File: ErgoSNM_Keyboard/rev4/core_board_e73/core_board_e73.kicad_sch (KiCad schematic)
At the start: 58 parts, among them J1 USB_C_Receptacle_USB2.0, J2 Conn_02x10_Odd_Even, J3 Conn_02x10_Odd_Even, J4 PJ-393_TRRS_8P, J5 PJ-393_TRRS_8P, J6 Conn_Batt, J7 Debug, J8 Conn_02x05_Odd_Even, J9 Conn_02x05_Odd_Even, SW1 SW_SPDT, SW2 SW_SPDT, U1 E73-2G4M08S1C, U2 USBLC6-2SC6, U3 BQ24075RGT, U4 TPS63900, Y1 32.768kHz

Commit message: feat: update E73 core board
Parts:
- removed C1: 4.7nF, Capacitor_SMD:C_0805_2012Metric, symbol Device:C_Small
- removed C10, C9: 4.7uF, Capacitor_SMD:C_0402_1005Metric, symbol Device:C_Small
- removed C11, C12: 22uF, Capacitor_SMD:C_0805_2012Metric, symbol Device:C_Small
- removed C4: 100nF, Capacitor_SMD:C_0402_1005Metric, symbol Device:C_Small
- removed C7: 1uF, Capacitor_SMD:C_0402_1005Metric, symbol Device:C_Small
- removed F1: 500mA, 6V, Fuse:Fuse_0805_2012Metric, symbol Device:Polyfuse
- removed H23, H5, H6, H7: MountingHole, ErgoSNM_Keyboard:mouse_bit, symbol Mechanical:MountingHole
- removed H3, H4: MountingHole, MountingHole:MountingHole_2.7mm_M2.5_ISO7380, symbol Mechanical:MountingHole
- removed J1: USB_C_Receptacle_USB2.0, Connector_USB:USB_C_Receptacle_HRO_TYPE-C-31-M-12, symbol Connector:USB_C_Receptacle_USB2.0
- removed J6: Conn_Batt, Connector_JST:JST_PH_S2B-PH-SM4-TB_1x02-1MP_P2.00mm_Horizontal, symbol Connector_Generic_MountingPin:Conn_01x02_MountingPin
- removed J8, J9: Conn_02x05_Odd_Even, Connector_PinHeader_1.27mm:PinHeader_2x04_P1.27mm_Vertical, symbol Connector_Generic:Conn_02x04_Odd_Even
- removed L1: 2.2uH, Inductor_SMD:L_Changjiang_FNR252012S, symbol Device:L
- removed R1: 1M, Resistor_SMD:R_0603_1608Metric, symbol Device:R_Small
- removed R10, R11, R7: 10k, Resistor_SMD:R_0402_1005Metric, symbol Device:R_Small
- removed R12: 1.2k 1%, Resistor_SMD:R_0603_1608Metric, symbol Device:R_Small
- removed R13: 0R 1%, Resistor_SMD:R_0603_1608Metric, symbol Device:R_Small
- removed R14: 30k 1%, Resistor_SMD:R_0603_1608Metric, symbol Device:R_Small
- removed R3, R4: 5.1k 1%, Resistor_SMD:R_0402_1005Metric, symbol Device:R
- removed R5: 2k, Resistor_SMD:R_0402_1005Metric, symbol Device:R_Small
- removed SB1: Charge Boost, Jumper:SolderJumper-2_P1.3mm_Open_TrianglePad1.0x1.5mm, symbol Jumper:SolderJumper_2_Open
- removed SB2: LiPo_CHG, Jumper:SolderJumper-2_P1.3mm_Open_TrianglePad1.0x1.5mm, symbol Jumper:SolderJumper_2_Open
- removed SB3: Vsrc Select, Jumper:SolderJumper-3_P2.0mm_Open_TrianglePad1.0x1.5mm_NumberLabels, symbol Jumper:SolderJumper_3_Open
- removed SB4: VDD Selection, Jumper:SolderJumper-3_P2.0mm_Open_TrianglePad1.0x1.5mm_NumberLabels, symbol Jumper:SolderJumper_3_Open
- removed SW1, SW2: SW_SPDT, ErgoSNM_Keyboard:9_3.5_3.5_switch, symbol Switch:SW_SPDT
- removed TP1: RST, TestPoint:TestPoint_Pad_D1.5mm, symbol Connector:TestPoint
- removed TP2: GND, TestPoint:TestPoint_Pad_D1.5mm, symbol Connector:TestPoint
- removed U2: USBLC6-2SC6, Package_TO_SOT_SMD:SOT-23-6, symbol Power_Protection:USBLC6-2SC6
- removed U3: BQ24075RGT, Package_DFN_QFN:VQFN-16-1EP_3x3mm_P0.5mm_EP1.6x1.6mm, symbol Battery_Management:BQ24075RGT
- removed U4: TPS63900, Package_SON:WSON-10-1EP_2.5x2.5mm_P0.5mm_EP1.2x2mm, symbol Regulator_Switching:TPS63900
- J2, J3: footprint Connector_PinHeader_1.27mm:PinHeader_2x10_P1.27mm_Vertical_SMD -> Connector_PinHeader_1.27mm:PinHeader_2x10_P1.27mm_Vertical
- J7: footprint ErgoSNM_Keyboard:SWD 10pin -> Connector_PinHeader_1.27mm:PinHeader_2x05_P1.27mm_Vertical
- U1: footprint ErgoSNM_Keyboard:E73-2G4M08S1C-52840_PCBA -> ErgoSNM_Keyboard:E73-2G4M08S1C-52840_Hand
- renumbered R8 to R10, R9 to R11, R6 to R5
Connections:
- net COL_IO_0: now also U1.10 (P0.30); no longer U1.8 (P0.29)
- net COL_IO_2: now also U1.8 (P0.29); no longer U1.10 (P0.30)
- net COL_IO_3: now also U1.38 (P1.02); no longer U1.15 (P0.05)
- net COL_IO_4: now also U1.40 (P1.04); no longer U1.17 (P1.09)
- net COL_IO_5: now also U1.42 (P1.06); no longer U1.22 (P0.07)
- net HS_IO_1: now also U1.30 (P0.17); no longer U1.35 (P0.24)
- net HS_IO_2: now also U1.32 (P0.20); no longer U1.34 (P0.22)
- net HS_IO_3: now also U1.34 (P0.22); no longer U1.32 (P0.20)
- net HS_IO_4: now also U1.36 (P1.00); no longer U1.30 (P0.17)
- net HS_IO_5: now also U1.35 (P0.24); no longer U1.36 (P1.00)
- no-connect marks 34 -> 28
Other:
- added sheet power (power.kicad_sch)
- note added: "REG0 bypass"
- note removed: "2xAA Battery or LiPo Battery"
- note removed: "Adafruit nRF52 Bootloader for nice!nano"
- note removed: "HIGH: VOUT Config 1 LOW: VOUT Config 2"
- note removed: "R_{ISET}(Ω)=890(AΩ)/I_{CHG}(A) R_{ISET} range: 590Ω ~ 8.9kΩ"
- note removed: "Refer to Nordic nRF52833-DK 4.7nF 10V"
- note removed: "USB"
- moved on the sheet: C2, C3, C5, C6, C8, H1, H2, J2, J3, J4, J5, J7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

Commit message: feat: update BOM
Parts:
- H1, H2, J2, J3, J7: MFR. Part # (none) -> --
- J5: now not fitted
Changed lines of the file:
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@@
+			)
+		)
+		(property "MFR. Part #" "--"
+			(at 156.21 184.15 0)
+			(effects
+				(font
+					(size 1.27 1.27)
+				)
+				(hide yes)
 			)
 		)
@@
 			)
 		)
+		(property "MFR. Part #" "--"
+			(at 138.43 153.67 0)
+			(effects
+				(font
+					(size 1.27 1.27)
+				)
+				(hide yes)
+			)
+		)
 		(pin "10"
 		)
@@
 			)
 		)
+		(property "MFR. Part #" "--"
+			(at 146.05 55.88 0)
+			(effects
+				(font
+					(size 1.27 1.27)
+				)
+				(hide yes)
+			)
+		)
 		(pin "1"
 		)
@@
 			)
 		)
+		(property "MFR. Part #" "--"
+			(at 146.05 92.71 0)
+			(effects
+				(font
+					(size 1.27 1.27)
+				)
+				(hide yes)
+			)
+		)
 		(pin "1"
 		)
@@
 		(in_bom yes)
 		(on_board yes)
-		(dnp no)
+		(dnp yes)
 		(property "Reference" "J5"
 			(at 234.95 73.66 0)
@@
 			(at 156.21 190.5 0)
 			(effects
+				(font
+					(size 1.27 1.27)
+				)
+				(hide yes)
+			)
+		)
+		(property "MFR. Part #" "--"
+			(at 156.21 190.5 0)
+			(effects

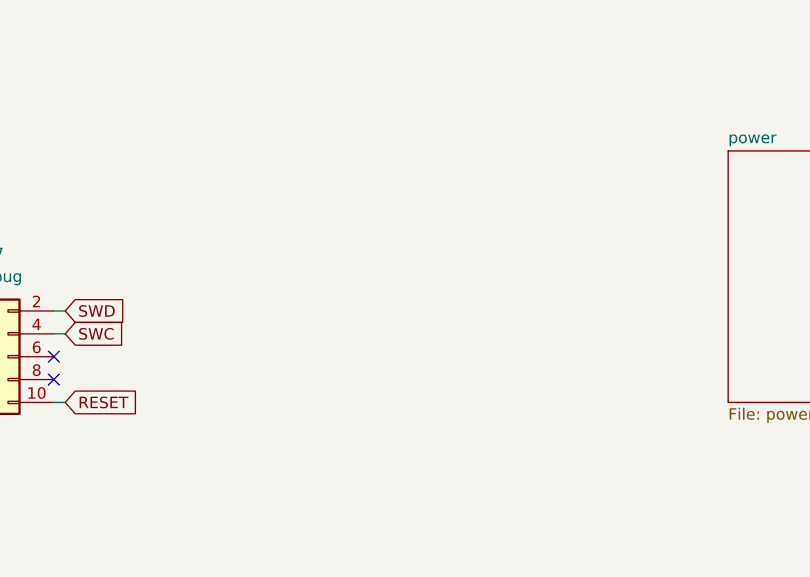
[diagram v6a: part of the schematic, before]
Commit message: feat: add stats and change LED
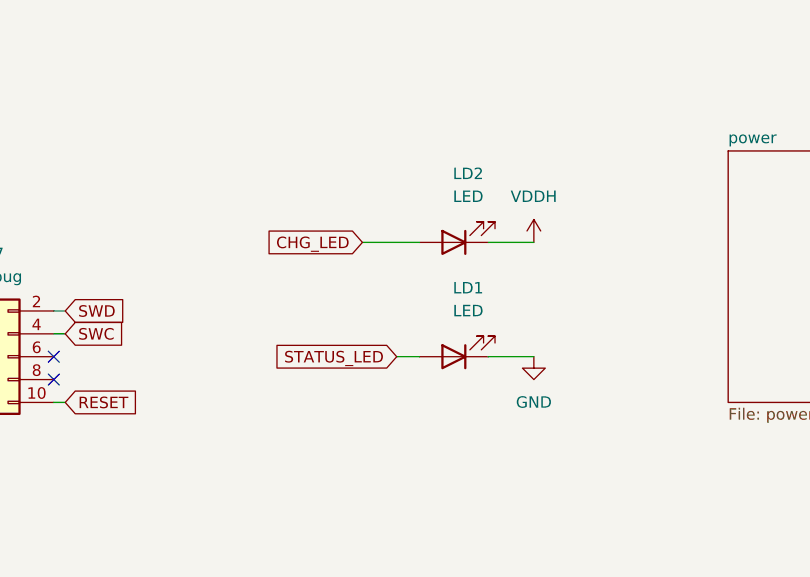
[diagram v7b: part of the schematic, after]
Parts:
- added LD1, LD2: LED, LED_SMD:LED_0603_1608Metric, symbol Device:LED
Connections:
- net CHG_LED: now also LD2.2 (A)
- net GND: now also LD1.1 (K)
- net STATUS_LED: now also LD1.2 (A)
- new net VDDH: LD2.1 (K)

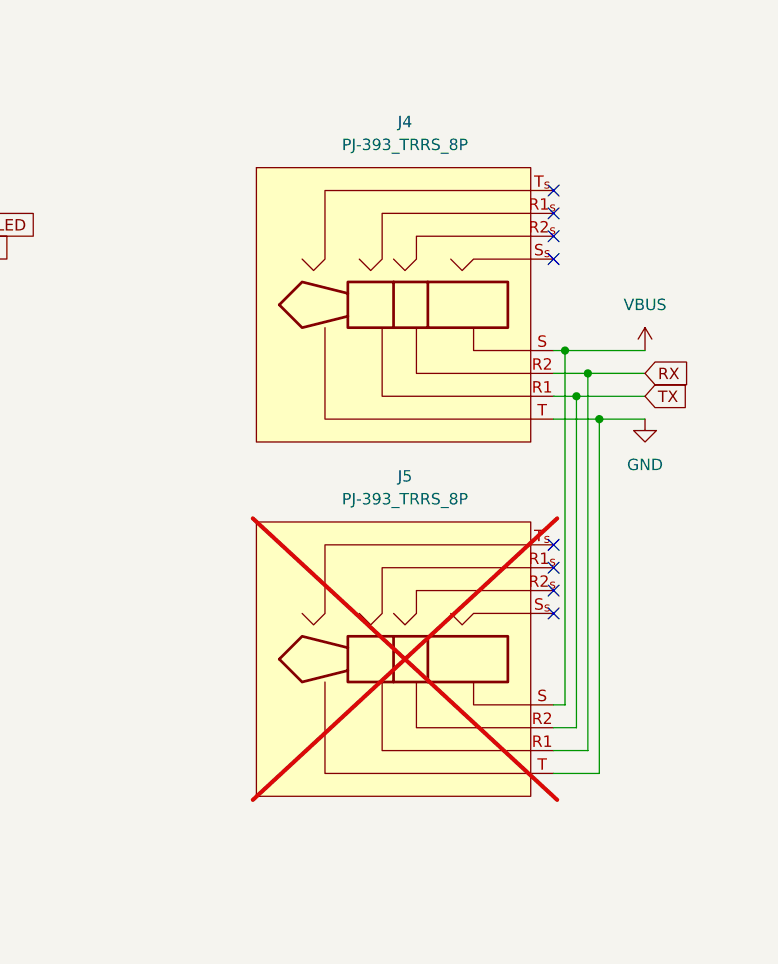
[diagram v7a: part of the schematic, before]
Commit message: feat: add 3D models (USB-C, TRRS, Switch)
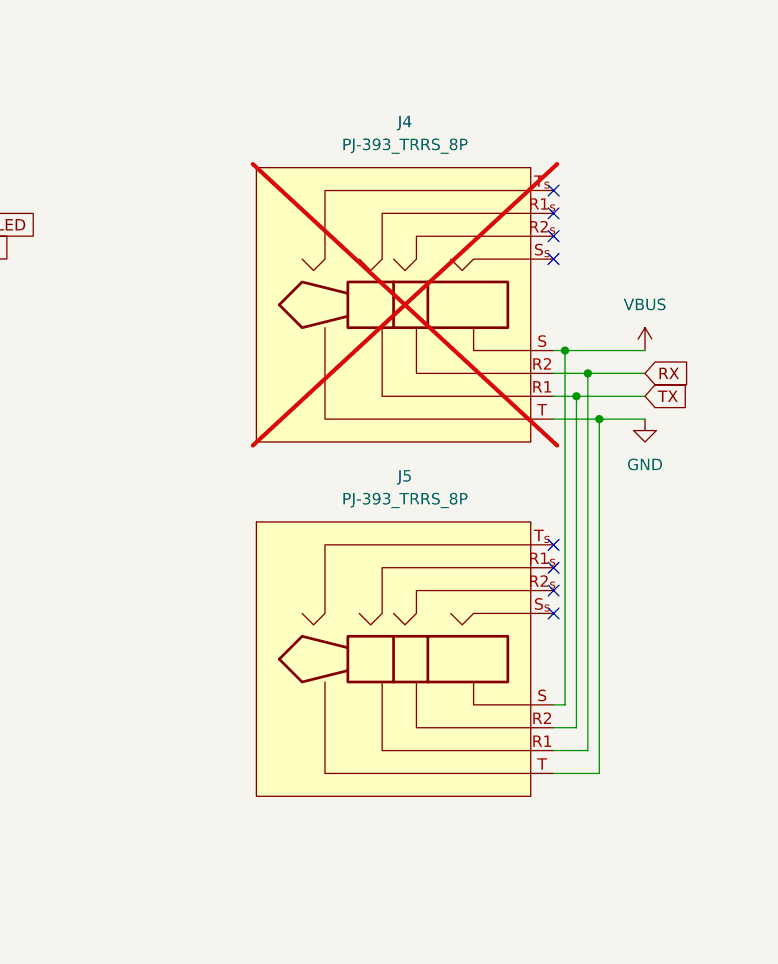
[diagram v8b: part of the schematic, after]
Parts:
- J4: now not fitted
- J5: now fitted
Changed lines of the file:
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@@
 		(in_bom yes)
 		(on_board yes)
-		(dnp no)
+		(dnp yes)
 		(property "Reference" "J4"
 			(at 234.95 34.29 0)
@@
 		(in_bom yes)
 		(on_board yes)
-		(dnp yes)
+		(dnp no)
 		(property "Reference" "J5"
 			(at 234.95 73.66 0)
